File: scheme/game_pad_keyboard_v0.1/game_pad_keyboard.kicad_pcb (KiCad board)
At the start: 2 copper layers, 70 x 99 mm, 209 parts, among them J1 USB, J2 GPIO, J3 SWD, M1 vibrator, Q1 BSS138, Q2 BSS138, Q3 BSS138, Q4 BSS138, Q5 BSS138, Q6 BSS138, Q7 BSS138, Q8 BSS138, SW1 SW_Push, SW10 SW_Push, SW11 SW_Push, SW12 SW_Push, SW13 SW_Push, SW14 Reset, SW15 Battery, SW2 SW_Push, SW3 SW_Push, SW4 SW_Push, SW5 Power, SW6 SW_Push, SW7 SW_Push, SW8 SW_Push, SW9 SW_Push, U1 LM75B, U10 ADM3485, U11 NRF24L01_Breakout, U12 MAX3232, U13 CH340G, U14 JDY-23, U2 AMS1117-3.3, U3 DS3231M, U4 TP5400, U5 74HC595, U6 74HC595, U7 74HC595, U8 STM32F103C6Tx, U9 74HC165, Y1 8MHz, Y2 12MHz

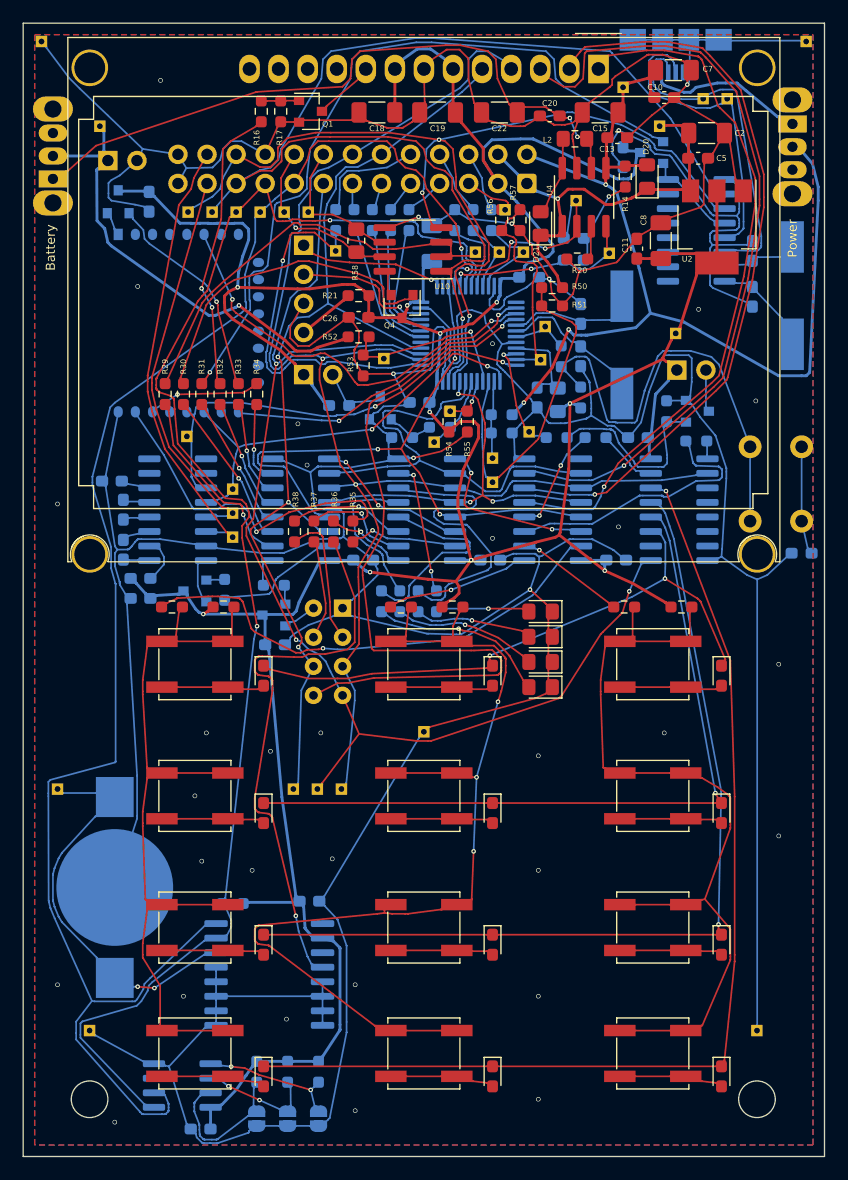
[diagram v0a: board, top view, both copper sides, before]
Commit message: fix: Caps location
Location of the capacitors has changed; they are
now located after the transistors.
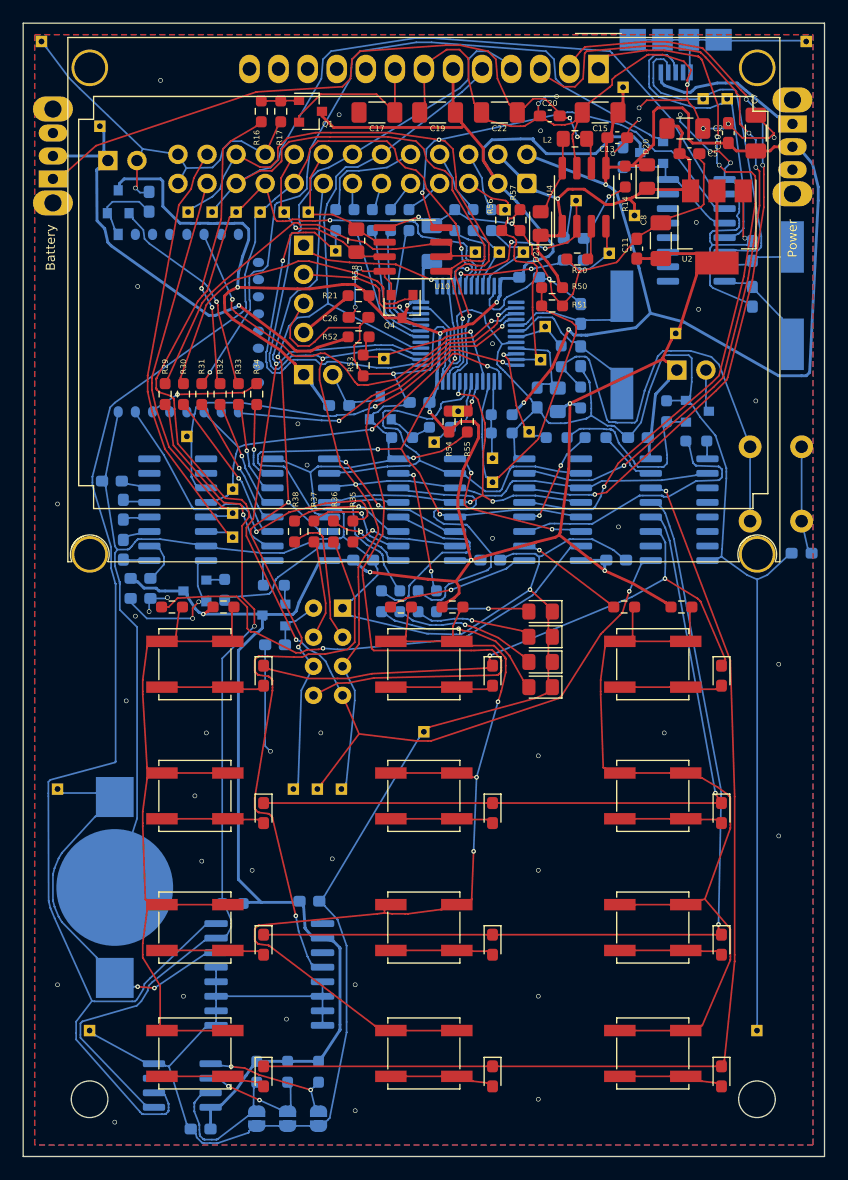
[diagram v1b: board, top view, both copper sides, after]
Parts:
- moved C7 9.06 mm to (174.0, 59.6), turned to 90 degrees
- moved TP13 8.10 mm to (163.4, 66.8)
- moved C10 6.40 mm to (171.6, 59.6), turned to 90 degrees
- moved C2 1.94 mm to (167.8, 59.2)
- moved C5 0.86 mm to (168.2, 61.4)
- moved TP4 0.70 mm to (148.0, 83.9)
- moved G*** 0.20 mm to (169.2, 141.4)
- turned G*** to 180 degrees
- renumbered C18 to C17, C17 to C18
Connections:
- C17 pad 1: +3V3 -> /display_anode
- C26 pad 1: +3V3 -> GND
- C26 pad 2: GND -> Net-(C26-Pad2)
- C27 pad 1: +3V3 -> GND
- C27 pad 2: GND -> Net-(C27-Pad2)
- C28 pad 1: +3V3 -> GND
- C28 pad 2: GND -> Net-(C28-Pad2)
- C34 pad 1: +3V3 -> GND
- C34 pad 2: GND -> Net-(C34-Pad2)
- C35 pad 1: +3V3 -> GND
- C35 pad 2: GND -> Net-(C35-Pad2)
- DS1 pad 8: +3V3 -> /display_anode
- DS1 pad 9: /display_cathode -> GND
- Q1 pad 2: GND -> /display_anode
- Q1 pad 3: /display_cathode -> +3V3
- Q4 pad 2: Net-(Q4-Pad2) -> Net-(C26-Pad2)
- Q5 pad 2: Net-(Q5-Pad2) -> Net-(C27-Pad2)
- Q6 pad 2: Net-(Q6-Pad2) -> Net-(C28-Pad2)
- Q7 pad 2: Net-(Q7-Pad2) -> Net-(C34-Pad2)
- Q8 pad 2: Net-(Q8-Pad2) -> Net-(C35-Pad2)
- U10 pad 8: Net-(Q4-Pad2) -> Net-(C26-Pad2)
- U11 pad 2: Net-(Q5-Pad2) -> Net-(C27-Pad2)
- U12 pad 16: Net-(Q6-Pad2) -> Net-(C28-Pad2)
- U13 pad 16: Net-(Q7-Pad2) -> Net-(C34-Pad2)
- U13 pad 4: Net-(Q7-Pad2) -> Net-(C34-Pad2)
- U14 pad 1: Net-(Q8-Pad2) -> Net-(C35-Pad2)
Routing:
- net VDD: track 91.0 -> 106.3 mm
- net /display_anode: track 0.00 -> 14.5 mm
- net Net-(C28-Pad2): track 0.00 -> 13.1 mm, vias 0 -> 2
- net Net-(C34-Pad2): track 0.00 -> 11.7 mm
- net Net-(C26-Pad2): track 0.00 -> 9.30 mm, vias 0 -> 2
- net Net-(Q7-Pad2): track 8.05 -> 0.00 mm
- net Net-(C35-Pad2): track 0.00 -> 6.88 mm
- net /display_cathode: track 5.48 -> 0.00 mm
- net +3V3: track 331.8 -> 336.7 mm
- net GND: track 645.7 -> 641.1 mm, vias 38 -> 57
- net Net-(C27-Pad2): track 0.00 -> 4.62 mm
- net Net-(Q6-Pad2): track 4.38 -> 0.00 mm
- net Net-(Q5-Pad2): track 2.96 -> 0.00 mm
- net Net-(Q4-Pad2): track 2.32 -> 0.00 mm
- net Net-(Q8-Pad2): track 2.13 -> 0.00 mm
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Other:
- board text added: "2023/11/14"
- board text removed: "2023/08/14"
